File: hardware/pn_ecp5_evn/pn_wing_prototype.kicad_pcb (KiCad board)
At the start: 2 copper layers, 240 parts, among them J101 Screw_Terminal_01x02, J102 Conn_Coaxial, J103 Conn_02x20_Odd_Even, J104 Conn_Coaxial, J105 Conn_Coaxial, J106 Conn_Coaxial, J107 Conn_01x10, J201 Conn_Coaxial, J301 Conn_Coaxial, J401 Conn_Coaxial, J601 Conn_Coaxial, J701 Conn_Coaxial, J702 Conn_Coaxial, J703 Conn_Coaxial, U201 VEMI65AB-HCI, U202 LMX2594, U301 PAT1220-C-3DB, U302 TRF37A73, U303 PAT1220-C-3DB, U401 PAT1220-C-3DB, U402 TRF37A73, U403 PAT1220-C-3DB, U501 LM27761, U502 ADM7171ACPZ-3.3-R7, U601 LM2904, U602 OPA2211, U701 SYM-63LH+, U702 ADG621, U703 OPA2211, U801 THS4551, U802 LT6657BHMS8-2.5, U901 ADS7868, U902 ADS7868, U903 Si8640BB-B-IU, U904 Si8640BB-B-IU, U905 Si8642BB-B-IU, X601 ABLNO

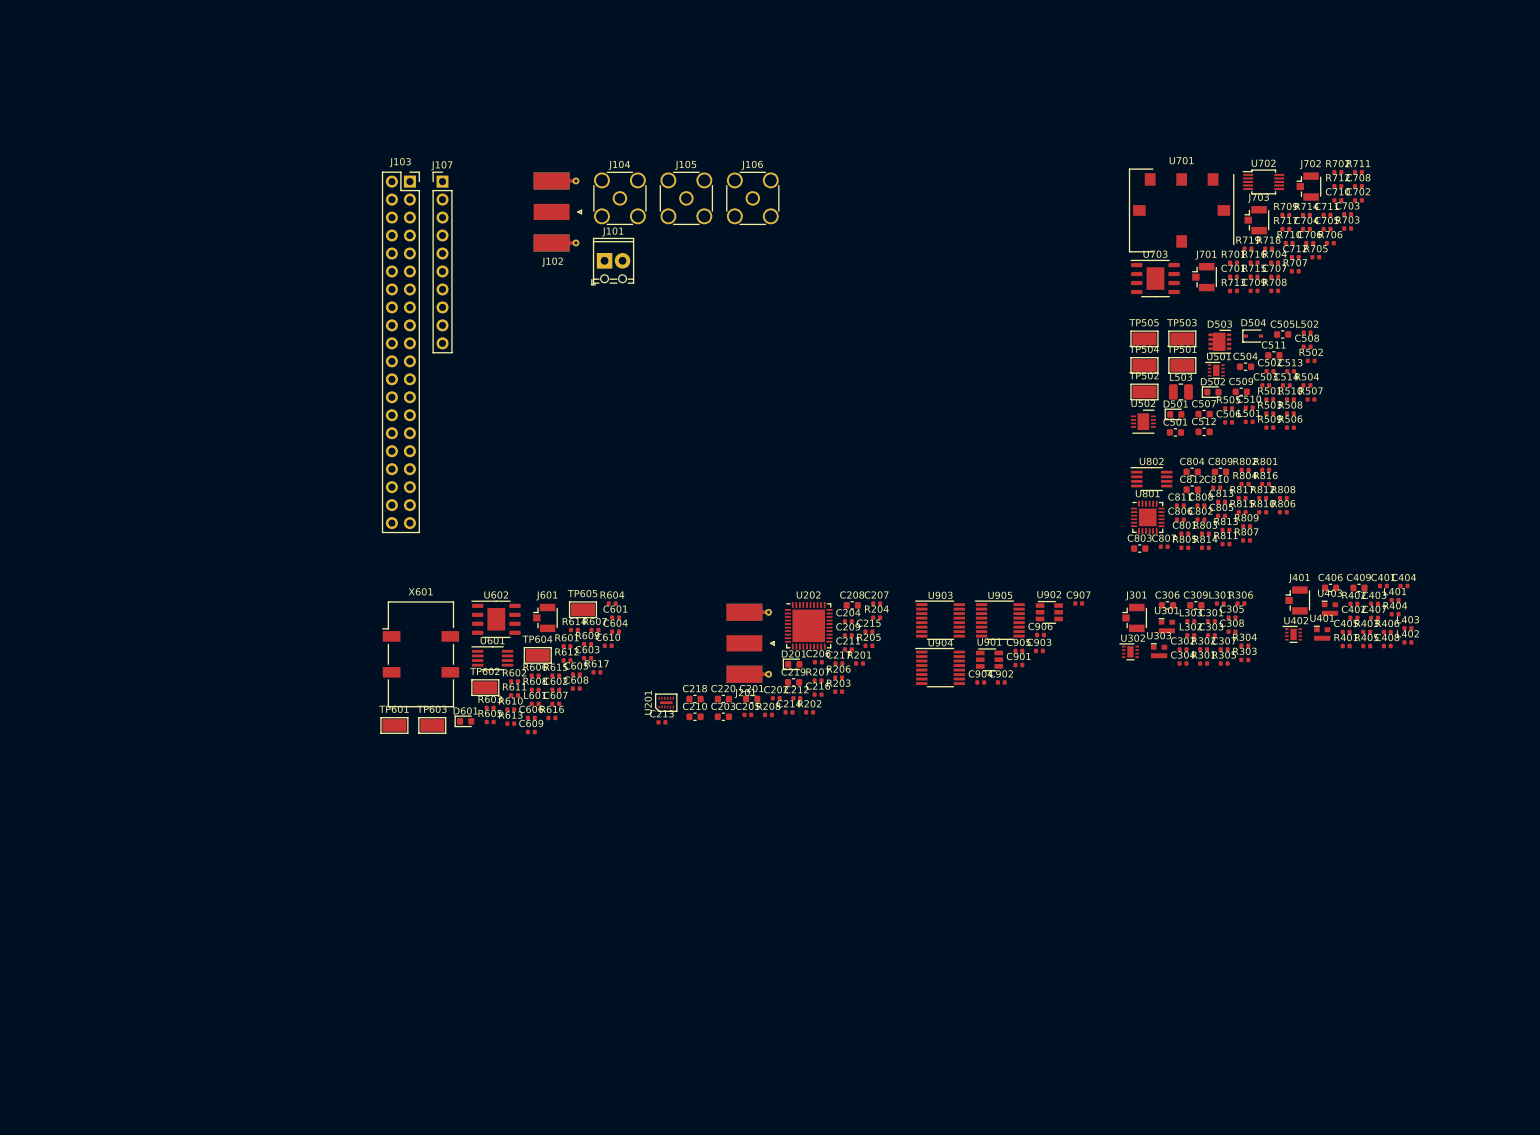
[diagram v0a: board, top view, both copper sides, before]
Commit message: started component placement on phase noise analyzer
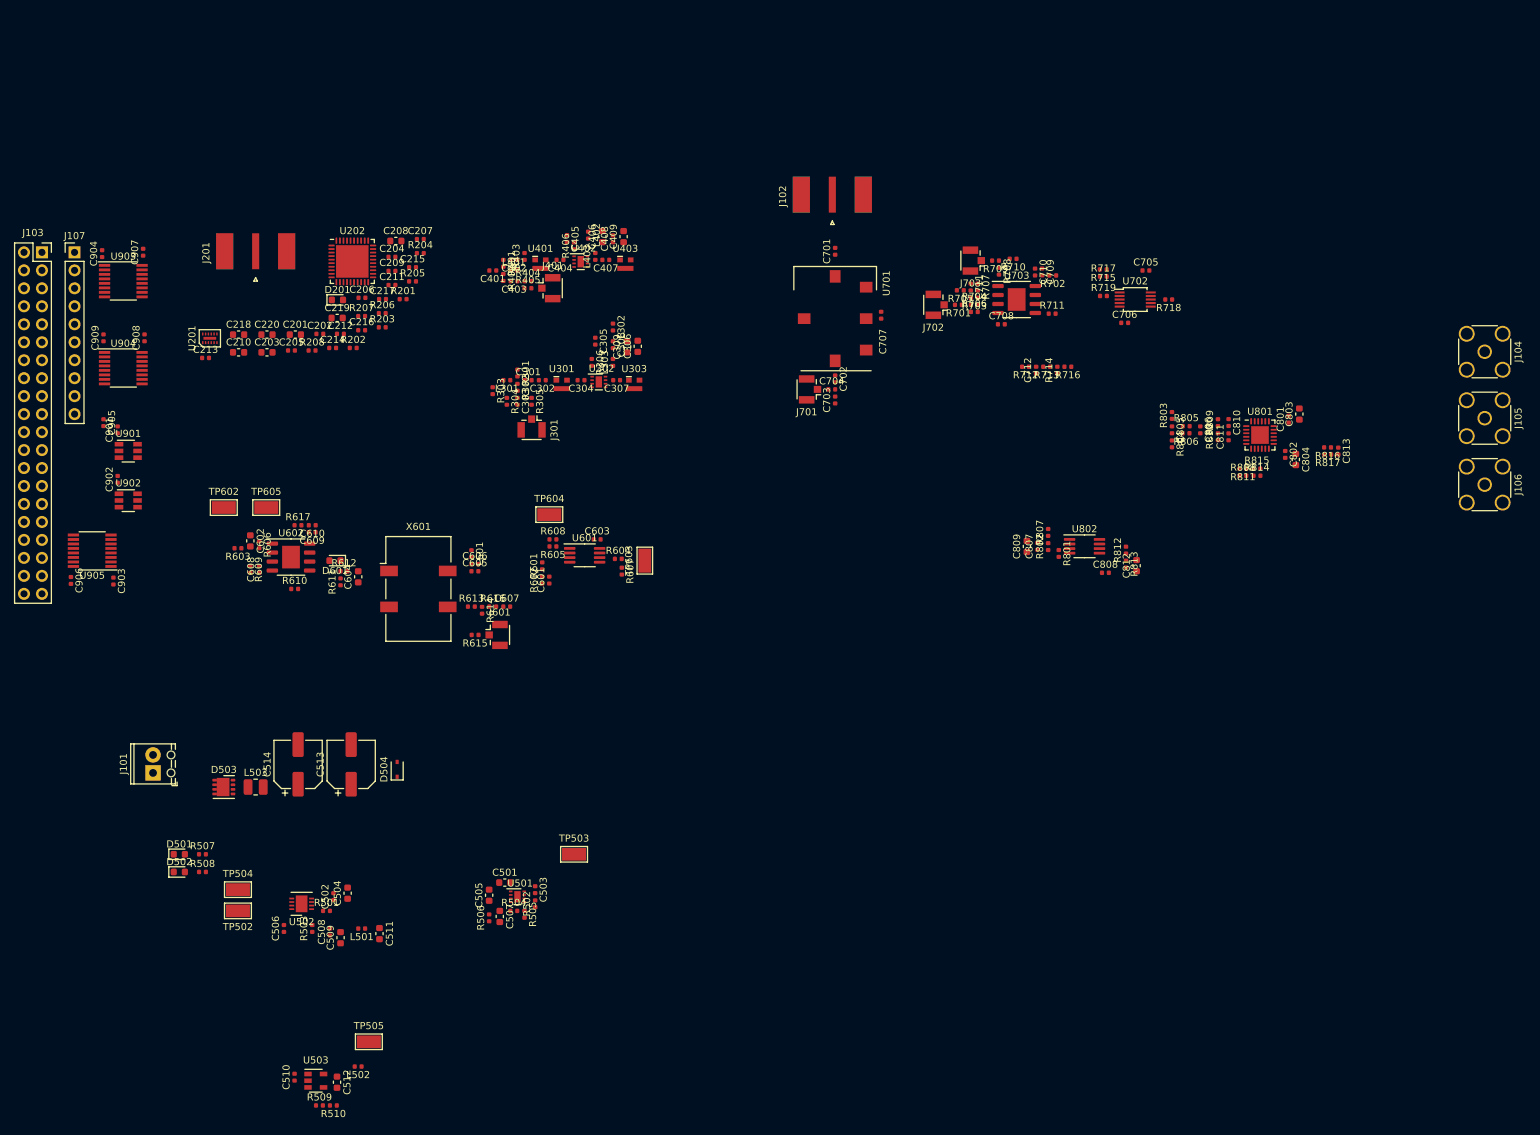
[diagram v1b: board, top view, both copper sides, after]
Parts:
- removed TP501, TP601: TestPoint, TestPoint:TestPoint_Keystone_5015_Micro-Minature
- added C908: 100 nF, Capacitor_SMD:C_0402_1005Metric, F.Cu at (48.3, 79.5)
- added C909: 100 nF, Capacitor_SMD:C_0402_1005Metric, F.Cu at (42.5, 79.5)
- added U503: TPS72301DB, Package_TO_SOT_SMD:SOT-23-5, F.Cu at (72.5, 184.5)
- C513, C514: value 100 uF -> 270 uF; footprint Capacitor_SMD:C_0402_1005Metric -> Capacitor_SMD:CP_Elec_6.3x5.9
- C602: footprint Capacitor_SMD:C_0402_1005Metric -> Capacitor_SMD:C_0603_1608Metric
- C604: value C_Small -> 1 uF; footprint Capacitor_SMD:C_0402_1005Metric -> Capacitor_SMD:C_0603_1608Metric
- C605: value C_Small -> 10 nF
- C606: value C_Small -> 1 uF
- C701: value C_Small -> 1 nF
- C703: value DNI -> 1 nF
- J102, J201: footprint Connector_Coaxial:SMA_Molex_73251-1153_EdgeMount_Horizontal -> vna:SMA_Molex_73251-1153_OSHFR408
- R610, R613, R616, R807: value R_Small -> 0
- R611: value R_Small -> 10k
- R612: value R_Small -> 100
- R614, R615: value R_Small -> DNI
- R812, R813: value R_Small -> 1k
- moved L502 169.5 mm to (78.5, 182.5), turned to 180 degrees
- moved R507 169.3 mm to (56.5, 152.5)
- moved R510 168.1 mm to (75.0, 188.0), turned to 180 degrees
- moved R508 166.8 mm to (56.5, 155.0)
- moved R509 165.0 mm to (73.0, 188.0)
- moved C510 164.8 mm to (69.5, 184.0), turned to 90 degrees
- moved D502 161.0 mm to (53.2, 155.0)
- moved C508 161.0 mm to (74.5, 163.5), turned to 90 degrees
- moved D503 154.2 mm to (59.5, 143.0)
- moved D501 153.9 mm to (53.2, 152.5)
- moved R503 153.6 mm to (72.0, 163.0), turned to 90 degrees
- moved C512 153.2 mm to (75.5, 184.7), turned to 270 degrees
- moved C502 151.8 mm to (75.0, 158.5), turned to 90 degrees
- moved R501 151.6 mm to (74.0, 160.5)
- moved C506 151.5 mm to (68.0, 163.0), turned to 90 degrees
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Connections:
- U702 pad 3: (no net) -> /IF_G2
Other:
- copper layers 2 -> 4
- net class Default: clearance 0.2 -> 0.15
- rule pad_to_mask_clearance: 0 -> 0.05
- rule trace_clearance: 0.2 -> 0.15
- rule trace_min: 0.2 -> 0.1
- rule via_min_drill: 0.3 -> 0.254
- rule via_min_size: 0.4 -> 0.45

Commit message: component placement on phase noise downconverter
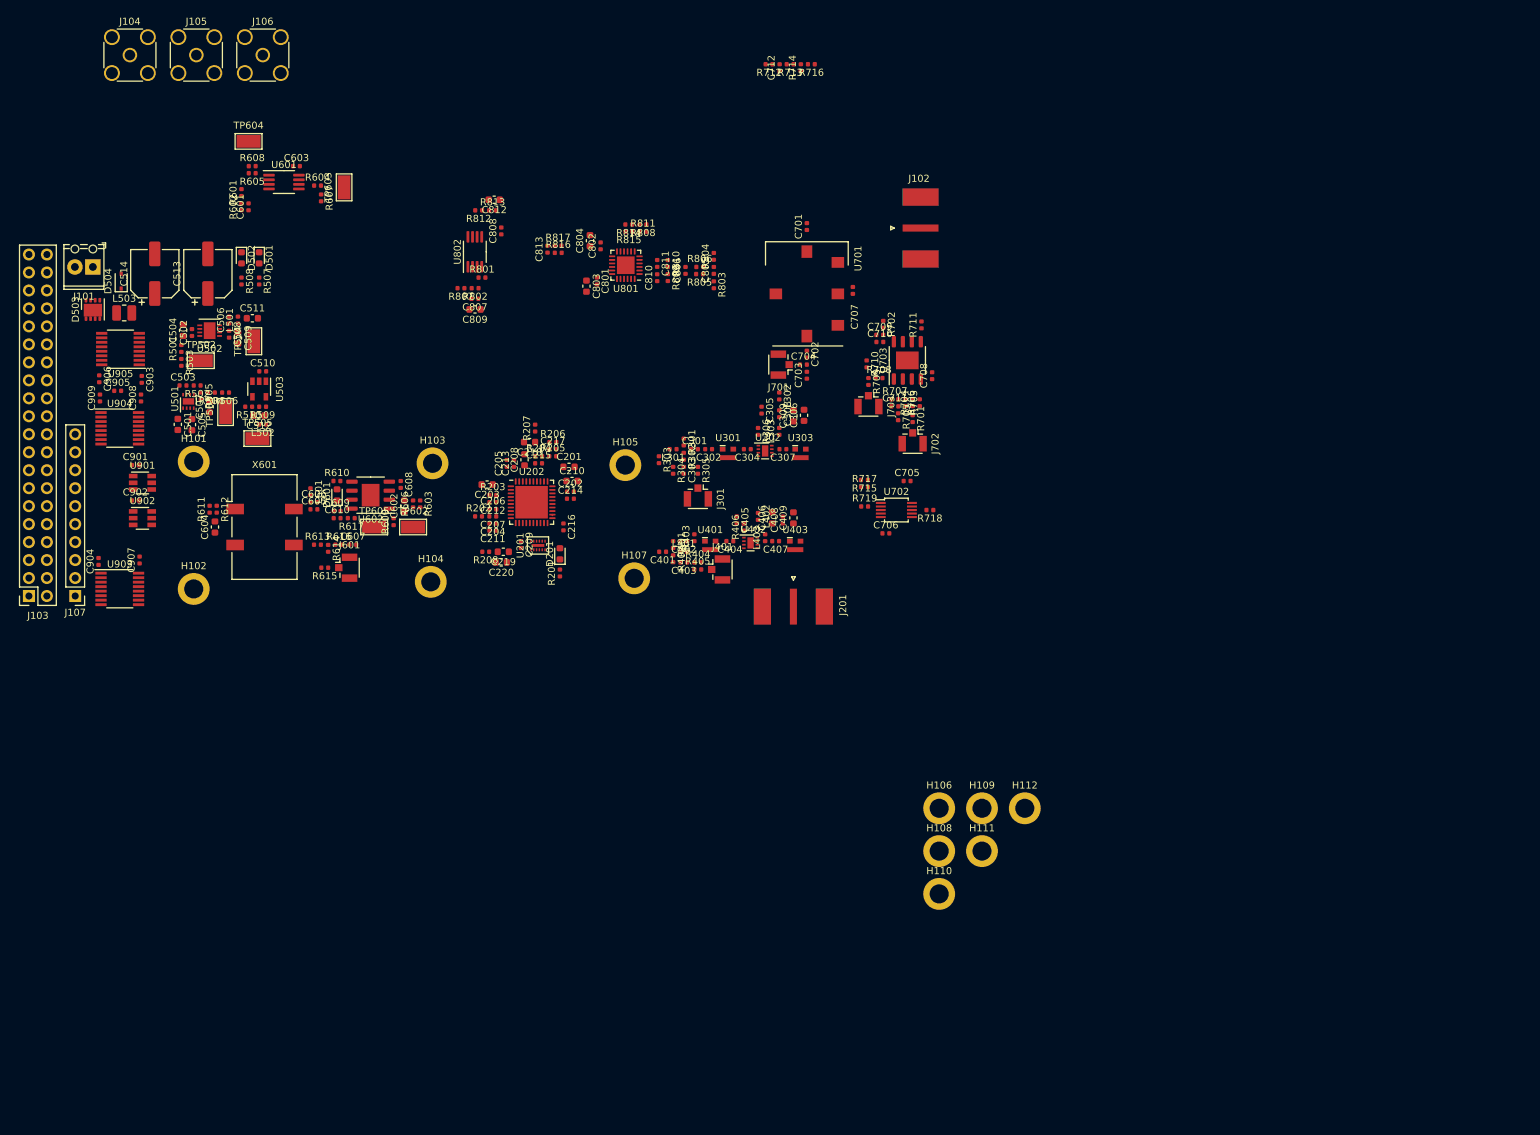
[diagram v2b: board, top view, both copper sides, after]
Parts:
- added H101: MountingHole_Pad, MountingHole:MountingHole_2.7mm_M2.5_ISO14580_Pad, F.Cu at (55.2, 97.0)
- added H102: MountingHole_Pad, MountingHole:MountingHole_2.7mm_M2.5_ISO14580_Pad, F.Cu at (55.2, 115.0)
- added H103: MountingHole_Pad, MountingHole:MountingHole_2.7mm_M2.5_ISO14580_Pad, F.Cu at (89.0, 97.2)
- added H104: MountingHole_Pad, MountingHole:MountingHole_2.7mm_M2.5_ISO14580_Pad, F.Cu at (88.8, 114.0)
- added H105: MountingHole_Pad, MountingHole:MountingHole_2.7mm_M2.5_ISO14580_Pad, F.Cu at (116.2, 97.5)
- added H106: MountingHole_Pad, MountingHole:MountingHole_2.7mm_M2.5_ISO14580_Pad, F.Cu at (160.6, 146.0)
- added H107: MountingHole_Pad, MountingHole:MountingHole_2.7mm_M2.5_ISO14580_Pad, F.Cu at (117.5, 113.5)
- added H108: MountingHole_Pad, MountingHole:MountingHole_2.7mm_M2.5_ISO14580_Pad, F.Cu at (160.6, 152.1)
- added H109: MountingHole_Pad, MountingHole:MountingHole_2.7mm_M2.5_ISO14580_Pad, F.Cu at (166.7, 146.0)
- added H110: MountingHole_Pad, MountingHole:MountingHole_2.7mm_M2.5_ISO14580_Pad, F.Cu at (160.6, 158.1)
- added H111: MountingHole_Pad, MountingHole:MountingHole_2.7mm_M2.5_ISO14580_Pad, F.Cu at (166.7, 152.1)
- added H112: MountingHole_Pad, MountingHole:MountingHole_2.7mm_M2.5_ISO14580_Pad, F.Cu at (172.7, 146.0)
- moved J104 196.0 mm to (46.2, 39.6), turned to 0 degrees
- moved J105 189.2 mm to (55.6, 39.6), turned to 0 degrees
- moved J106 183.0 mm to (65.0, 39.6), turned to 0 degrees
- moved C813 115.3 mm to (105.2, 67.0), turned to 90 degrees
- moved R817 112.7 mm to (106.7, 66.5), turned to 0 degrees
- moved R816 112.1 mm to (106.8, 67.5), turned to 0 degrees
- moved C812 104.5 mm to (97.7, 60.0), turned to 180 degrees
- moved C804 104.4 mm to (111.2, 65.8), turned to 90 degrees
- moved R812 103.3 mm to (95.5, 61.5), turned to 180 degrees
- moved R813 102.5 mm to (97.5, 61.5), turned to 0 degrees
- moved C803 102.4 mm to (110.8, 72.2), turned to 270 degrees
- moved C802 101.1 mm to (112.8, 66.5), turned to 90 degrees
- moved C510 99.9 mm to (65.0, 84.2), turned to 0 degrees
- moved C801 99.7 mm to (112.2, 71.5), turned to 270 degrees
- moved R510 99.5 mm to (63.0, 89.2)
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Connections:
- U202 pad 18: /synth/lo_amp/IN_N -> /synth/aux_output/IN_N
- U202 pad 19: /synth/lo_amp/IN_P -> /synth/aux_output/IN_P
- U202 pad 22: /synth/aux_output/IN_N -> /synth/lo_amp/IN_N
- U202 pad 23: /synth/aux_output/IN_P -> /synth/lo_amp/IN_P

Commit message: first pass component placement on phase noise downconverter
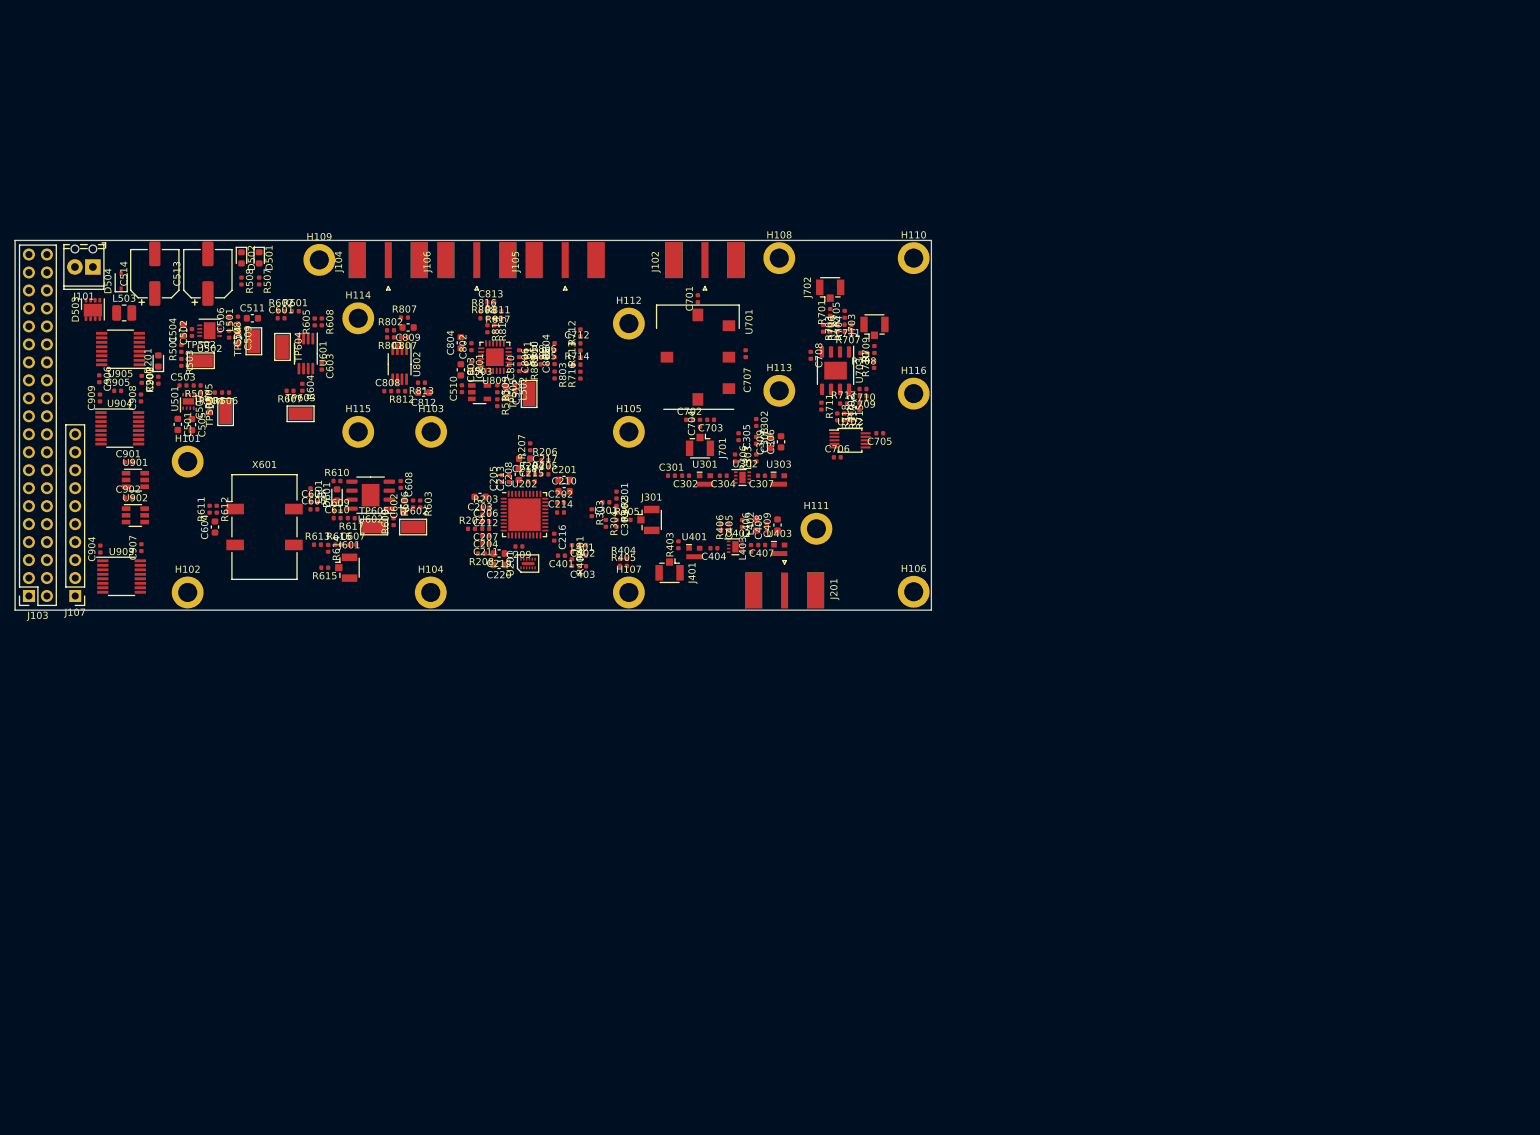
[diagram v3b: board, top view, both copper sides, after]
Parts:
- added H113: MountingHole_Pad, MountingHole:MountingHole_2.7mm_M2.5_ISO14580_Pad, F.Cu at (138.0, 87.0)
- added H114: MountingHole_Pad, MountingHole:MountingHole_2.7mm_M2.5_ISO14580_Pad, F.Cu at (78.5, 76.8)
- added H115: MountingHole_Pad, MountingHole:MountingHole_2.7mm_M2.5_ISO14580_Pad, F.Cu at (78.5, 92.8)
- added H116: MountingHole_Pad, MountingHole:MountingHole_2.7mm_M2.5_ISO14580_Pad, F.Cu at (157.0, 87.4)
- J104, J105, J106: footprint Connector_Coaxial:SMA_Amphenol_132134_Vertical -> vna:SMA_Molex_73251-1153_OSHFR408
- moved H109 121.6 mm to (73.0, 68.5)
- moved H110 89.9 mm to (157.0, 68.2)
- moved H112 88.4 mm to (116.8, 77.5)
- moved H108 86.8 mm to (138.0, 68.2)
- moved D201 63.0 mm to (50.2, 82.8)
- moved R201 63.0 mm to (50.2, 85.5)
- moved J105 60.5 mm to (107.8, 70.2), turned to 270 degrees
- moved R716 54.7 mm to (109.9, 84.8), turned to 90 degrees
- moved R714 52.6 mm to (109.4, 83.3), turned to 0 degrees
- moved H111 51.2 mm to (143.2, 106.5)
- moved R713 50.5 mm to (109.9, 81.8), turned to 90 degrees
- moved C712 48.4 mm to (109.4, 80.3), turned to 0 degrees
- moved J104 47.7 mm to (82.8, 70.2), turned to 270 degrees
- moved R712 46.4 mm to (109.9, 78.8), turned to 90 degrees
- moved J106 43.1 mm to (95.2, 70.2), turned to 270 degrees
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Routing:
- added copper zone on In1.Cu, net GND
- added copper zone on In1.Cu, net GNDD
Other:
- board outline added: 129.5 x 52.2 mm
